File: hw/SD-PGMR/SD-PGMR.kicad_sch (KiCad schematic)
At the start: 18 parts, among them J1 Conn_01x03 HDR, U1 AES-Pico, U2 74HCT574, U20 SST39SF040, U3 74LCX574, U4 74HCT191, U5 74HCT191, U6 74HCT191, U7 74HCT191, U8 74HCT191

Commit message: PCB v1.0 (ordered)
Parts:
- removed C13: 0.1uF, symbol Device:C_Small
- removed J1: Conn_01x03 HDR, symbol Connector_Generic:Conn_01x03
- added C1, C10: 0.1uF, Capacitor_SMD:C_0603_1608Metric_Pad1.08x0.95mm_HandSolder, symbol Device:C_Small
- added C4: 10uf, Capacitor_SMD:C_0603_1608Metric_Pad1.08x0.95mm_HandSolder, symbol Device:C_Small
- added H1, H2, H3, H4: MountingHole, MountingHole:MountingHole_2.2mm_M2, symbol Mechanical:MountingHole
- added J1: CONN_01x07 Socket, Connector_PinSocket_2.54mm:PinSocket_1x07_P2.54mm_Vertical, symbol Connector_Generic:Conn_01x07
- added J2, J4: Conn_01x03 HDR, Connector_PinHeader_2.54mm:PinHeader_1x03_P2.54mm_Vertical, symbol Connector_Generic:Conn_01x03
- added J3: J-V3.3, Connector_PinHeader_2.54mm:PinHeader_1x02_P2.54mm_Vertical, symbol Connector_Generic:Conn_01x02
- added LED1: GRN, LED_THT:LED_D5.0mm, symbol Device:LED
- added LED2: YEL, LED_THT:LED_D5.0mm, symbol Device:LED
- added LED3: RED, LED_THT:LED_D5.0mm, symbol Device:LED
- added Q1: MMBT3906, Package_TO_SOT_SMD:SOT-23, symbol Transistor_BJT:BC807
- added Q2: MMBT3904, Package_TO_SOT_SMD:SOT-23, symbol Transistor_BJT:MMBT3904
- added Q3: DMG2305UX, Package_TO_SOT_SMD:SOT-23, symbol AES_Library:DMG2305UX-AES
- added R1, R3: 1k, Resistor_SMD:R_0805_2012Metric_Pad1.20x1.40mm_HandSolder, symbol Device:R_US
- added R2, R6, R7: 450, Resistor_SMD:R_0805_2012Metric_Pad1.20x1.40mm_HandSolder, symbol Device:R_Small_US
- added R4: 20k, Resistor_SMD:R_0805_2012Metric_Pad1.20x1.40mm_HandSolder, symbol Device:R_US
- added R5: 4.7k, Resistor_SMD:R_0805_2012Metric_Pad1.20x1.40mm_HandSolder, symbol Device:R_Small_US
- added RE1: RotEnc-SW, Rotary_Encoder:RotaryEncoder_Alps_EC11E-Switch_Vertical_H20mm_MountingHoles, symbol Device:RotaryEncoder_Switch
- added SD1: MicroSD-Socket, AES_Library:AES-SDCard-GCT_MEM2075-00-140-01-A, symbol Connector:Micro_SD_Card_Det1
- added SW1, SW2: SW PB-MOM, AES_Library:AES-SW_PUSH_SMD_1P1T_NO_45x45mm-CK, symbol Switch:SW_Push
- added U4: 74HCT138, Package_SO:SOIC-16_3.9x9.9mm_P1.27mm, symbol 74xx:74LS138
- C2: renamed from C5; footprint (none) -> Capacitor_SMD:C_0603_1608Metric_Pad1.08x0.95mm_HandSolder
- C3: renamed from C6; footprint (none) -> Capacitor_SMD:C_0603_1608Metric_Pad1.08x0.95mm_HandSolder
- C5: renamed from C16; footprint (none) -> Capacitor_SMD:C_0603_1608Metric_Pad1.08x0.95mm_HandSolder
- C6: renamed from C1; footprint (none) -> Capacitor_SMD:C_0603_1608Metric_Pad1.08x0.95mm_HandSolder
- C7: renamed from C2; footprint (none) -> Capacitor_SMD:C_0603_1608Metric_Pad1.08x0.95mm_HandSolder
- C8: renamed from C3; footprint (none) -> Capacitor_SMD:C_0603_1608Metric_Pad1.08x0.95mm_HandSolder
- C9: renamed from C4; footprint (none) -> Capacitor_SMD:C_0603_1608Metric_Pad1.08x0.95mm_HandSolder
- U1: renamed from U2; footprint (none) -> Package_SO:SOIC-20W_7.5x12.8mm_P1.27mm
- U10: renamed from U20; value SST39SF040 -> SST39SF0n0; footprint (none) -> Socket:DIP_Socket-32_W11.9_W12.7_W15.24_W17.78_W18.5_3M_232-1285-00-0602J
- U2: renamed from U3; footprint (none) -> Package_SO:SOIC-20W_7.5x12.8mm_P1.27mm
- U3: renamed from U1; footprint RPi_Pico:RPi_Pico_SMD_TH -> AES_Library:AES-RPi_Pico_SMD_TH
- U5: renamed from U4; footprint (none) -> Package_SO:SOIC-16_3.9x9.9mm_P1.27mm
- U6: renamed from U5; footprint (none) -> Package_SO:SOIC-16_3.9x9.9mm_P1.27mm
- U7: renamed from U6; footprint (none) -> Package_SO:SOIC-16_3.9x9.9mm_P1.27mm
- U8: renamed from U7; footprint (none) -> Package_SO:SOIC-16_3.9x9.9mm_P1.27mm
- U9: renamed from U8; footprint (none) -> Package_SO:SOIC-16_3.9x9.9mm_P1.27mm
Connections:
- net +3.3V: now also U3.36 (3V3), J1.2 (Pin_2), J3.2 (Pin_2), R5.1, R6.1, SD1.4 (VDD)
- net +5V: now also U3.39 (VSYS), U3.40 (VBUS), Q1.3 (C), Q3.3 (D), R4.2, U4.16 (VCC), U4.6 (E3); no longer U10.32 (VCC)
- net GND: now also U3.23 (GND), U3.28 (GND), U3.33 (AGND), U3.38 (GND), C1.2, C10.1, C4.2, J1.1 (Pin_1), J2.1 (Pin_1), J3.1 (Pin_1), J4.1 (Pin_1), LED1.1 (K), LED2.1 (K), LED3.1 (K), Q2.2 (E), RE1.C, RE1.S1, SD1.10 (SHIELD), SD1.6 (VSS), SW1.2, SW2.2, U4.4 (E1), U4.5 (E2), U4.8 (GND)
- net PD0: now also U3.14 (GPIO10)
- net PD1: now also U3.15 (GPIO11)
- net PD2: now also U3.16 (GPIO12), J4.3 (Pin_3)
- net PD3: now also U3.17 (GPIO13), J4.2 (Pin_2)
- net PD4: now also U3.19 (GPIO14)
- net PD5: now also U3.20 (GPIO15)
- net PD6: now also U3.21 (GPIO16)
- net PD7: now also U3.22 (GPIO17)
- net ADM_LD-: now reaches U7.11 (~{LD}), U8.11 (~{LD})
- net ADM_LD-: now also U4.13 (O2)
- net ACLK: now reaches U5.14 (CLK), U6.14 (CLK), U7.14 (CLK), U8.14 (CLK), U9.14 (CLK)
- net ACLK: now also U4.7 (O7)
- net SD_DET-: now reaches U3.10 (GPIO7)
- net SD_DET-: now also SD1.9 (DET)
- net RE_SW-: now reaches U3.11 (GPIO8)
- net RE_SW-: now also C1.1, RE1.S2
- net FPWR_ON: now reaches U3.12 (GPIO9)
- net FPWR_ON: now also R1.1, R3.1
- net PRD-: now reaches U3.24 (GPIO18)
- net PRD-: now also U10.24 (OE), U2.1 (OE)
- net PWR-: now reaches U3.25 (GPIO19)
- net PWR-: now also U1.1 (OE)
- net DATA_LCH: now reaches U3.26 (GPIO20)
- net DATA_LCH: now also U1.11 (Cp), U2.11 (Cp)
- net FWR-: now reaches U3.27 (GPIO21)
- net FWR-: now also U10.31 (PGM)
- net at U3.29 (GPIO22): now also SW2.1
- net RESET-: now reaches U3.30 (RUN)
- net RESET-: now also C4.1, R5.2, SW1.1
- net A0: now reaches U3.31 (GPIO26_ADC0)
- net A0: now also U4.3 (A2)
- net A1: now reaches U3.32 (GPIO27_ADC1)
- net A1: now also U4.2 (A1)
- net A2: now reaches U3.34 (GPIO28_ADC2)
- net A2: now also U4.1 (A0)
- net CARD_CS-: now reaches U3.7 (GPIO5)
- net CARD_CS-: now also SD1.2 (DAT3/CD)
- net DISP_CS-: now reaches U3.9 (GPIO6)
- net DISP_CS-: now also J1.7 (Pin_7)
- net ADH_LD-: now reaches U9.11 (~{LD})
- net ADH_LD-: now also U4.12 (O3)
- net F_SEL-: now reaches U10.22 (CE)
- net F_SEL-: now also U4.11 (O4)
- net ADL_LD-: now reaches U5.11 (~{LD}), U6.11 (~{LD})
- net ADL_LD-: now also U4.14 (O1)
- net BA19: no longer names the net of U9.7 (Q3)
- net RXD renamed RE_B
- net RE_B: now also J2.2 (Pin_2), RE1.B
- net SPI0_CLK renamed SPICK
- net SPICK: now also J1.3 (Pin_3), SD1.5 (CLK)
- net SPI0_MISO renamed SPIMI
- net SPIMI: now also SD1.7 (DAT0)
- net SPI0_MOSI renamed SPIMO
- net SPIMO: now also J1.4 (Pin_4), SD1.3 (CMD)
- net TXD renamed RE_A
- net RE_A: now also J2.3 (Pin_3), RE1.A
- new net: Q2.1 (B), R3.2
- new net: Q2.3 (C), Q3.1 (G), R4.1
- new net: Q1.1 (B), R1.2
- new net: Q1.2 (E), R2.1
- new net: LED2.2 (A), R6.2
- new net: LED3.2 (A), R7.2
- new net: LED1.2 (A), R2.2
- new net +5VP: C10.2, Q3.2 (S), R7.1, U10.32 (VCC)
- new net DISPRST-: J1.5 (Pin_5), U4.10 (O5)
- new net DISP_CD: J1.6 (Pin_6), U4.9 (O6)
- no-connect marks 3 -> 15
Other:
- note added: "3.3V Sourced from Pico"
- note added: "5V Sourced from USB"
- moved on the sheet: C2, C3, C5, C6, C7, C8, C9, U1, U10, U2, U3, U5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

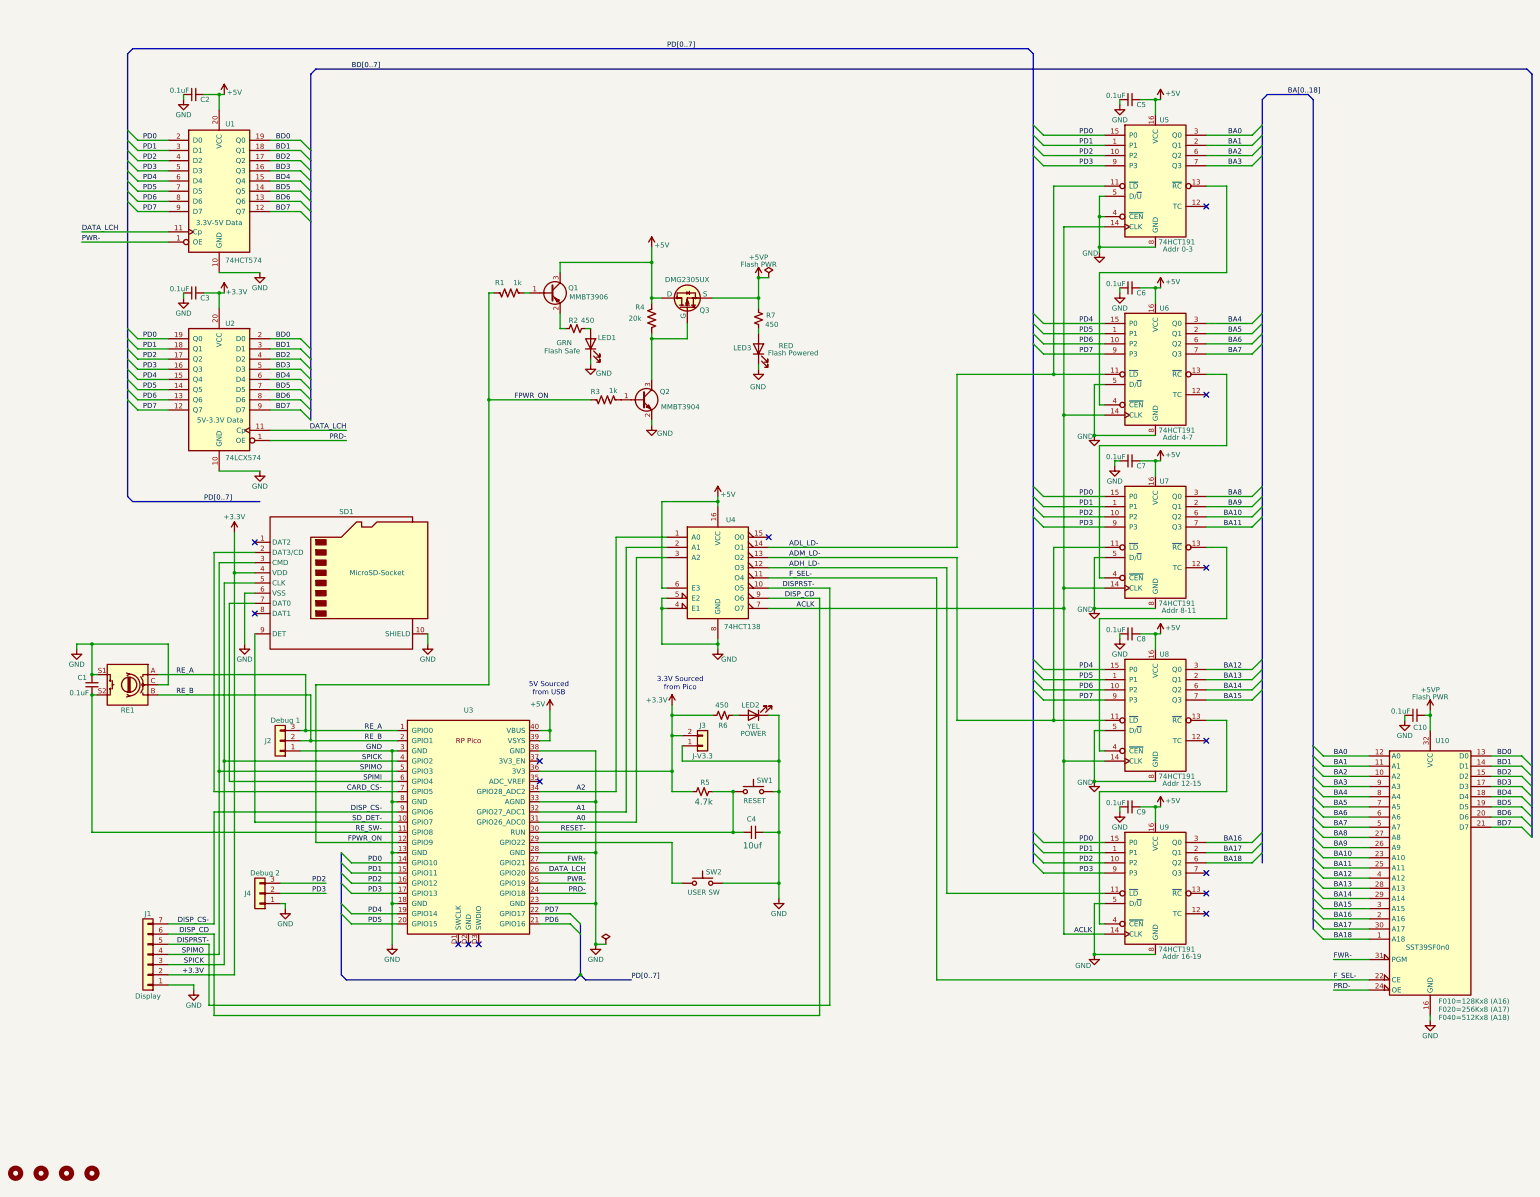
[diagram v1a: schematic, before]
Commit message: PGMR: Last of this PCB. New version needed for device power.
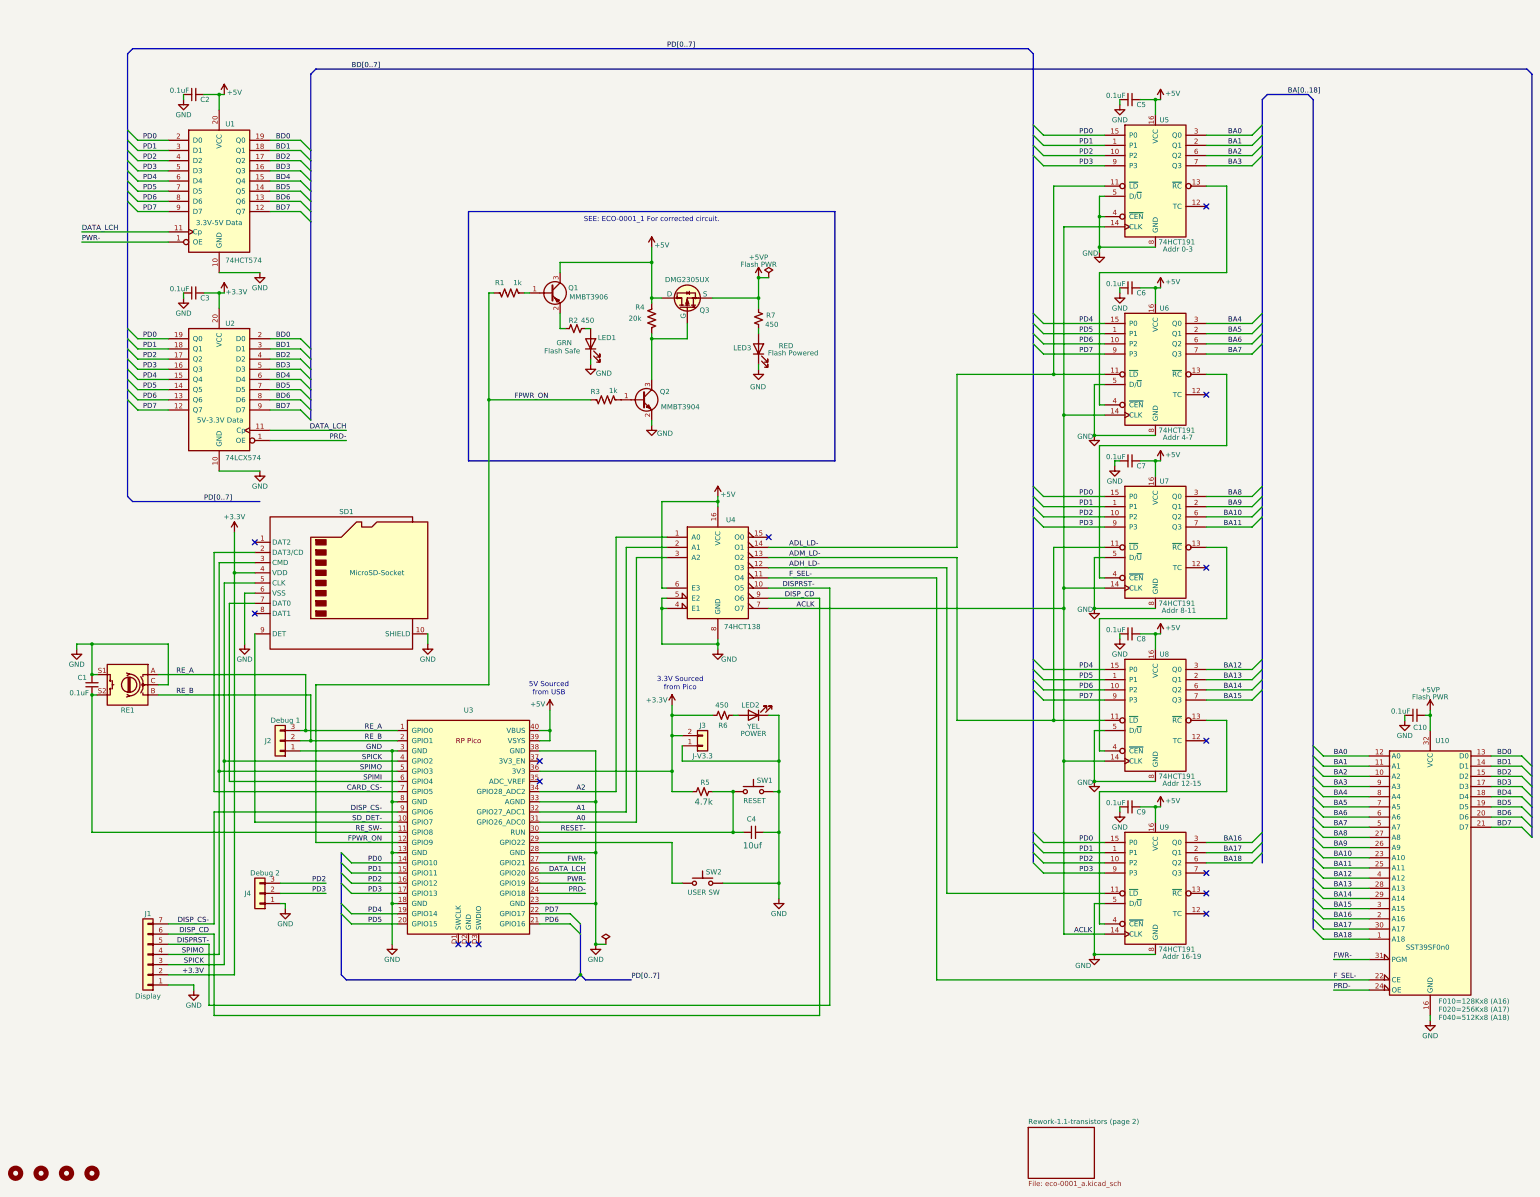
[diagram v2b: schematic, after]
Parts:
- LED1, LED3, Q1, Q2, Q3, R1, R2, R3, R4, R7: now left out of the parts list
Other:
- added sheet Rework-1.1-transistors (page 2) (eco-0001_a.kicad_sch)
- note added: "SEE: ECO-0001_1 For corrected circuit."
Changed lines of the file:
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@@
 		(comment 1 "Copyright 2025 AES")
 	)
+	(rectangle
+		(start 130.81 66.04)
+		(end 222.25 128.27)
+		(stroke
+			(width 0)
+			(type solid)
+			(color 194 0 0 1)
+		)
+		(fill
+			(type color)
+			(color 194 194 194 0.2)
+		)
+	)
 	(text "3.3V Sourced\nfrom Pico"
 		(exclude_from_sim no)
@@
 		)
 	)
+	(text "SEE: ECO-0001_1 For corrected circuit."
+		(exclude_from_sim no)
+		(at 176.53 68.072 0)
+		(effects
+			(font
+				(size 1.27 1.27)
+				(color 194 0 0 1)
+			)
+		)
+	)
 	(text "5V Sourced\nfrom USB"
 		(exclude_from_sim no)
@@
 		(unit 1)
 		(exclude_from_sim no)
-		(in_bom yes)
-		(on_board yes)
+		(in_bom no)
+		(on_board no)
 		(dnp no)
 		(property "Reference" "Q2"
@@
 		(unit 1)
 		(exclude_from_sim no)
-		(in_bom yes)
-		(on_board yes)
+		(in_bom no)
+		(on_board no)
 		(dnp no)
 		(property "Reference" "R4"
@@
 		(unit 1)
 		(exclude_from_sim no)
-		(in_bom yes)
-		(on_board yes)
+		(in_bom no)
+		(on_board no)
 		(dnp no)
 		(property "Reference" "Q1"
@@
 		(unit 1)
 		(exclude_from_sim no)
-		(in_bom yes)
-		(on_board yes)
+		(in_bom no)
+		(on_board no)
 		(dnp no)
 		(property "Reference" "#PWR017"
@@
 		(unit 1)
 		(exclude_from_sim no)
-		(in_bom yes)
-		(on_board yes)
+		(in_bom no)
+		(on_board no)
 		(dnp no)
 		(property "Reference" "#PWR016"
@@
 		(unit 1)
 		(exclude_from_sim no)
-		(in_bom yes)
-		(on_board yes)
+		(in_bom no)
+		(on_board no)
 		(dnp no)
 		(property "Reference" "#PWR021"
@@
 		(unit 1)
 		(exclude_from_sim no)
-		(in_bom yes)
-		(on_board yes)
+		(in_bom no)
+		(on_board no)
 		(dnp no)
 		(property "Reference" "#FLG02"
@@
 		(unit 1)
 		(exclude_from_sim no)
-		(in_bom yes)
-		(on_board yes)
+		(in_bom no)
+		(on_board no)
 		(dnp no)
 		(property "Reference" "#PWR022"
@@
 		(unit 1)
 		(exclude_from_sim no)
-		(in_bom yes)
-		(on_board yes)
+		(in_bom no)
+		(on_board no)
 		(dnp no)
 		(property "Reference" "R7"
@@
 		(unit 1)
 		(exclude_from_sim no)
-		(in_bom yes)
-		(on_board yes)
+		(in_bom no)
+		(on_board no)
 		(dnp no)
 		(property "Reference" "Q3"
@@
 		(unit 1)
 		(exclude_from_sim no)
-		(in_bom yes)
-		(on_board yes)
+		(in_bom no)
+		(on_board no)
 		(dnp no)
 		(property "Reference" "#PWR014"
@@
 		(unit 1)
 		(exclude_from_sim no)
-		(in_bom yes)
-		(on_board yes)
+		(in_bom no)
+		(on_board no)
 		(dnp no)
 		(property "Reference" "R2"
@@
 		(unit 1)
 		(exclude_from_sim no)
-		(in_bom yes)
-		(on_board yes)
+		(in_bom no)
+		(on_board no)
 		(dnp no)
 		(property "Reference" "LED1"
@@
 		(unit 1)
 		(exclude_from_sim no)
-		(in_bom yes)
-		(on_board yes)
+		(in_bom no)
+		(on_board no)
 		(dnp no)
 		(property "Reference" "R3"
@@
 		(unit 1)
 		(exclude_from_sim no)
-		(in_bom yes)
-		(on_board yes)
+		(in_bom no)
+		(on_board no)
 		(dnp no)
 		(property "Reference" "LED3"
@@
 		(unit 1)
 		(exclude_from_sim no)
-		(in_bom yes)
-		(on_board yes)
+		(in_bom no)
+		(on_board no)
 		(dnp no)
 		(property "Reference" "R1"
@@
 				)
 			)
+		)
+	)
+	(sheet
+		(at 270.51 294.64)
+		(size 16.51 12.7)
+		(exclude_from_sim no)
+		(in_bom yes)
+		(on_board yes)
+		(dnp no)
+		(fields_autoplaced yes)
+		(stroke
+			(width 0.1524)
+			(type solid)
+		)
+		(fill
+			(color 0 0 0 0.0000)
+		)
+		(property "Sheetname" "Rework-1.1-transistors (page 2)"
+			(at 270.51 293.9284 0)
+			(effects
+				(font
+					(size 1.27 1.27)
+				)
+				(justify left bottom)
+			)
+		)
+		(property "Sheetfile" "eco-0001_a.kicad_sch"
+			(at 270.51 307.9246 0)
+			(effects
+				(font
+					(size 1.27 1.27)
+				)
+				(justify left top)
+			)
+		)
+		(instances
+			(project "SD-PGMR"
+				(path "/e911f333-789e-45e5-911e-dcecec8cc0e7"
+					(page "2")
+				)
+			)
